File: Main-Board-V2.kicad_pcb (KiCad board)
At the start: 2 copper layers, 200 x 70 mm, 74 parts, among them IC1 REG1117-5, J2 776280-1, J3 776280-1, J4 1-776163-5, K1 J107F1AS123VDC.36, K2 J107F1AS123VDC.36, K3 J107F1AS123VDC.36, K4 J107F1AS123VDC.36, K5 J107F1AS123VDC.36, Q1 2N2222A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

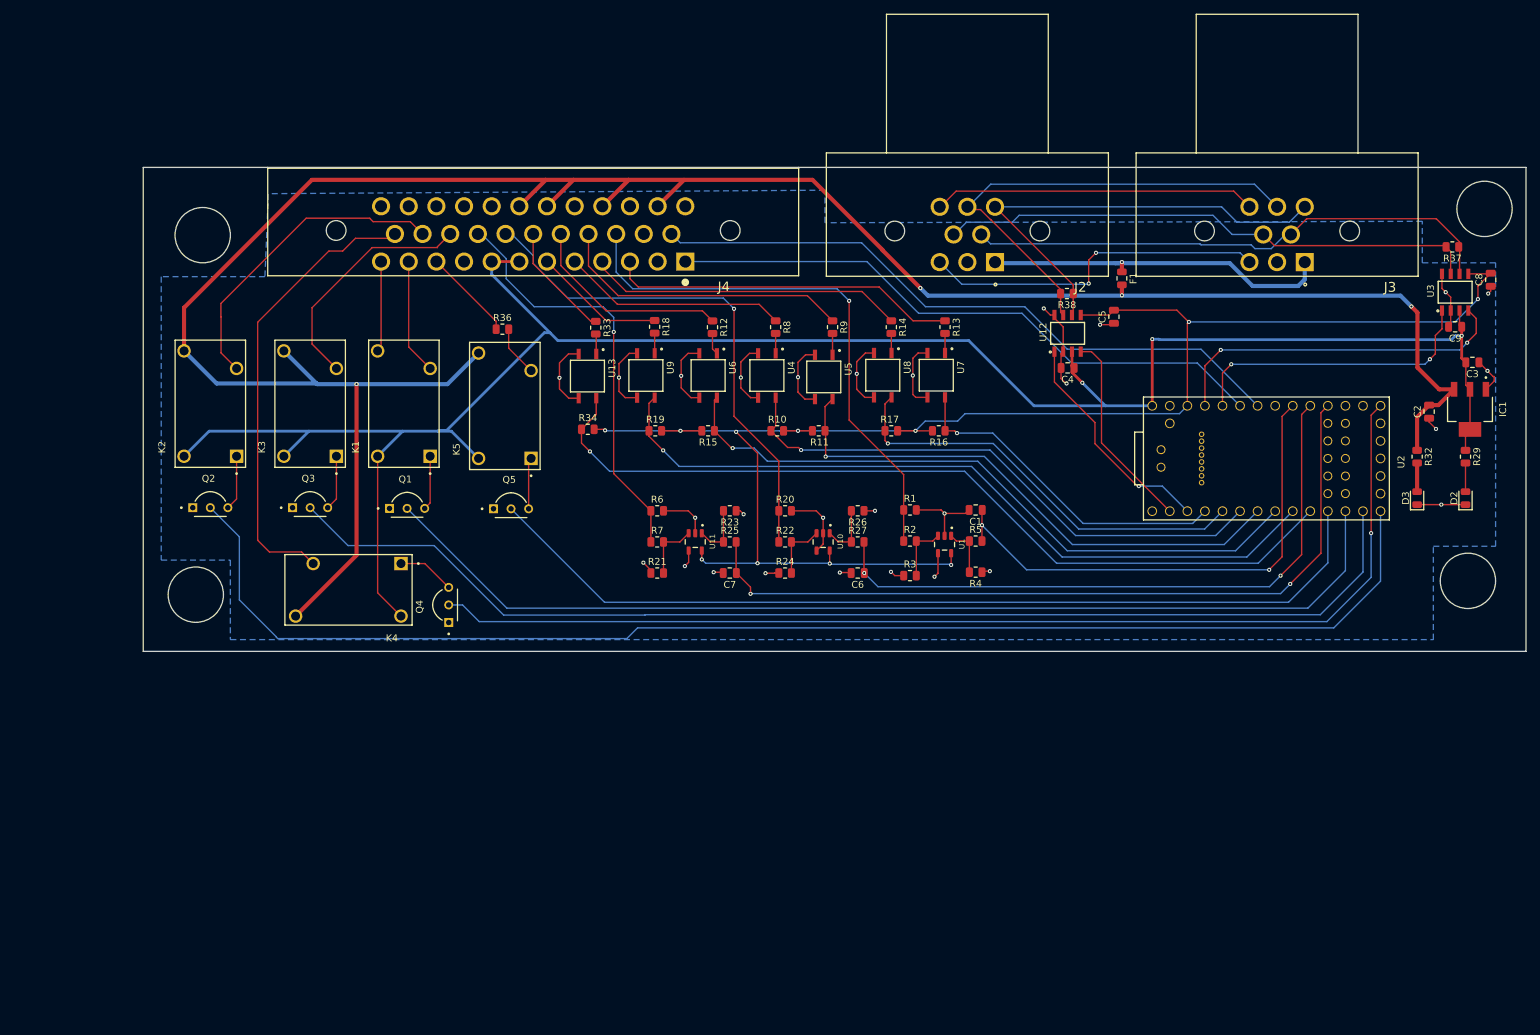
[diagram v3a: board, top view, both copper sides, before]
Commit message: fixed mounting holes
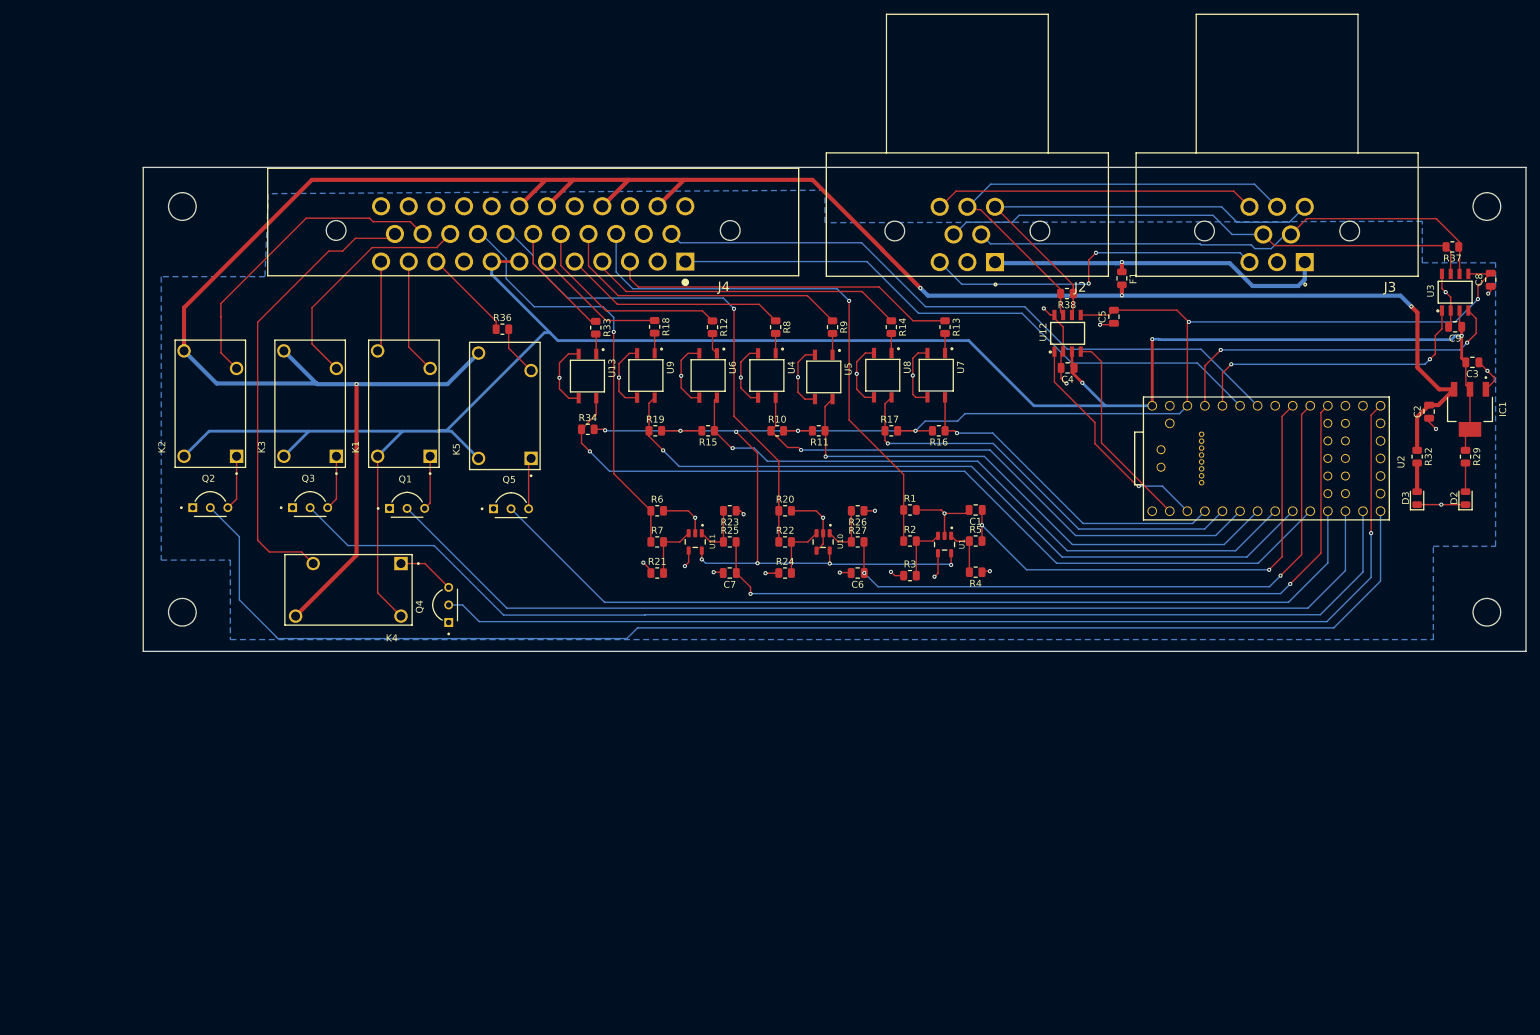
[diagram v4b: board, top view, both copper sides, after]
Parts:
- added REF**: MountingHole_4mm, MountingHole:MountingHole_4mm, F.Cu at (240.2, 125.5)
- added REF**: MountingHole_4mm, MountingHole:MountingHole_4mm, F.Cu at (240.2, 66.8)
- added REF**: MountingHole_4mm, MountingHole:MountingHole_4mm, F.Cu at (51.5, 66.8)
- added REF**: MountingHole_4mm, MountingHole:MountingHole_4mm, F.Cu at (51.5, 125.5)
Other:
- outline, holes or cut-outs redrawn

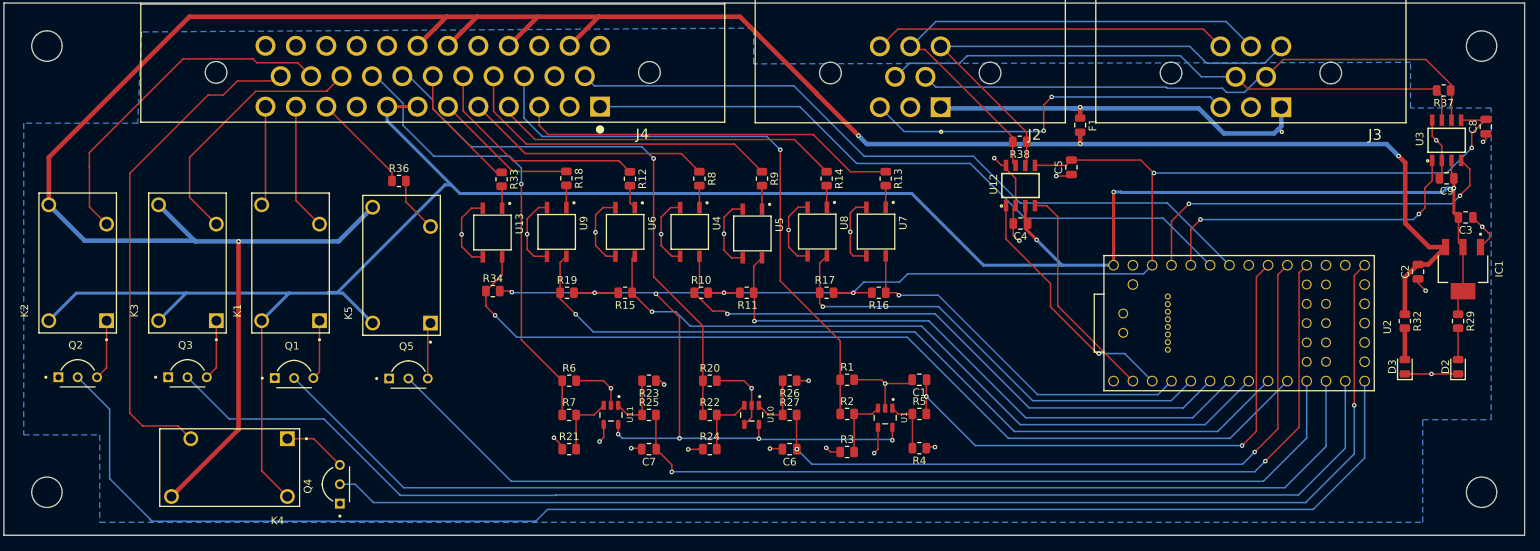
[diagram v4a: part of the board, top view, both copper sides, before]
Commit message: front silkscreen
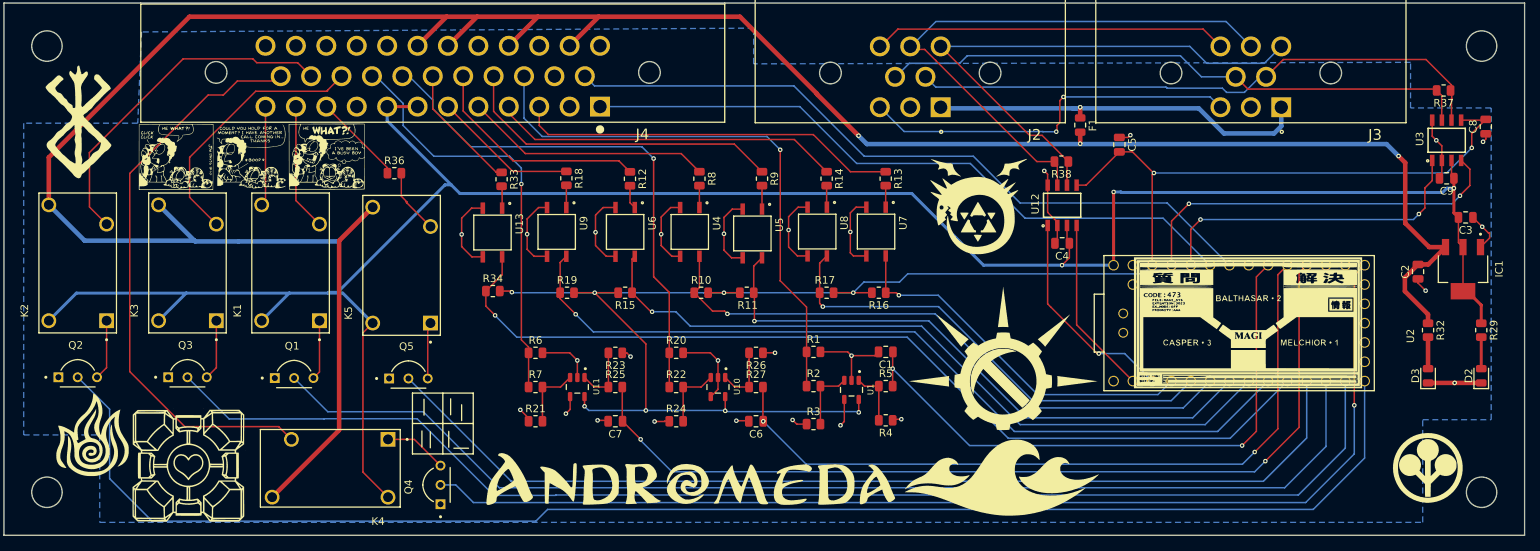
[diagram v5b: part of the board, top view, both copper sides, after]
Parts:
- removed the G*** at (142.0, 96.5)
- added G***: LOGO, LOGO, F.Cu at (177.1, 123.6)
- added G***: LOGO, LOGO, F.Cu at (174.1, 88.0)
- added G***: LOGO, LOGO, B.Cu at (212.3, 126.9)
- added G***: LOGO, LOGO, B.Cu at (233.2, 122.3)
- added G***: LOGO, LOGO, B.Cu at (126.4, 100.6)
- added G***: LOGO, LOGO, F.Cu at (177.3, 107.9)
- added G***: LOGO, LOGO, F.Cu at (209.5, 103.2)
- added G***: LOGO, LOGO, F.Cu at (57.5, 118.0)
- added G***: LOGO, LOGO, F.Cu at (78.5, 81.4)
- added G***: LOGO, LOGO, F.Cu at (70.2, 122.0)
- added G***: LOGO, LOGO, F.Cu at (55.7, 76.8)
- added G***: LOGO, LOGO, F.Cu at (233.2, 122.3)
- added G***: LOGO, LOGO, F.Cu at (136.3, 123.9)
- C1, C6, C7: value 1N -> 0.1U
- R21, R24: value 10k -> 20k
- R3: value 10k -> 30k
- R5: value 1k -> 1000R
- moved K4 13.2 mm to (88.8, 122.4)
- moved Q4 13.2 mm to (101.0, 124.6)
- moved C5 6.97 mm to (192.6, 79.8), turned to -90 degrees
- moved C4 6.07 mm to (185.1, 92.8)
- moved R38 6.07 mm to (185.0, 82.0)
- moved U12 6.07 mm to (185.1, 87.8)
- moved R21 5.75 mm to (115.8, 116.2)
- moved R6 5.75 mm to (115.8, 107.2)
- moved R7 5.75 mm to (115.8, 111.7)
- moved U11 5.75 mm to (121.3, 111.7)
- moved C7 5.75 mm to (126.3, 116.2)
- moved R23 5.75 mm to (126.3, 107.2)
- moved R25 5.75 mm to (126.3, 111.7)
- moved C1 5.75 mm to (161.9, 107.1)
- moved C6 5.75 mm to (144.8, 116.2)
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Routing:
- net /RightSignalIO: track 162.5 -> 149.2 mm
- net /Relays/RightSignal: track 65.2 -> 75.3 mm
- net +12V: track 340.1 -> 349.0 mm, vias 4 -> 3
- net /Can/CaNH1: track 69.1 -> 75.4 mm
- net /Can/CaNL1: track 66.8 -> 72.9 mm
- net /EncoderIO: track 73.8 -> 79.7 mm
- net /Throttle2IO: track 92.5 -> 98.5 mm
- net /Can_RX1: track 29.3 -> 23.5 mm
- net +3.3V: track 243.7 -> 238.1 mm, vias 11 -> 10
- net /Pedal/Throttle2: track 73.7 -> 68.2 mm
- net /Pedal/Throttle1: track 60.5 -> 55.0 mm
- net /Encoder: track 79.0 -> 73.5 mm
- net /Throttle1IO: track 115.0 -> 120.4 mm
- net /Can_TX1: track 33.1 -> 28.3 mm
- net GND: track 155.6 -> 153.3 mm, vias 28 -> 27
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
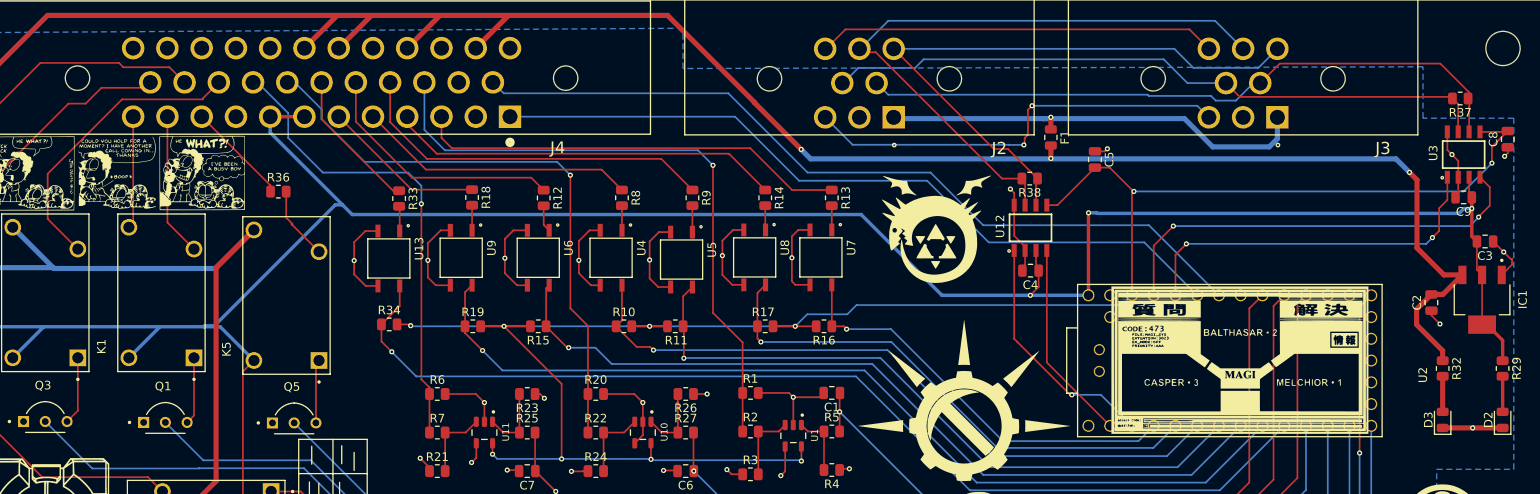
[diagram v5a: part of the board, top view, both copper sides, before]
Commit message: finished silkscreen
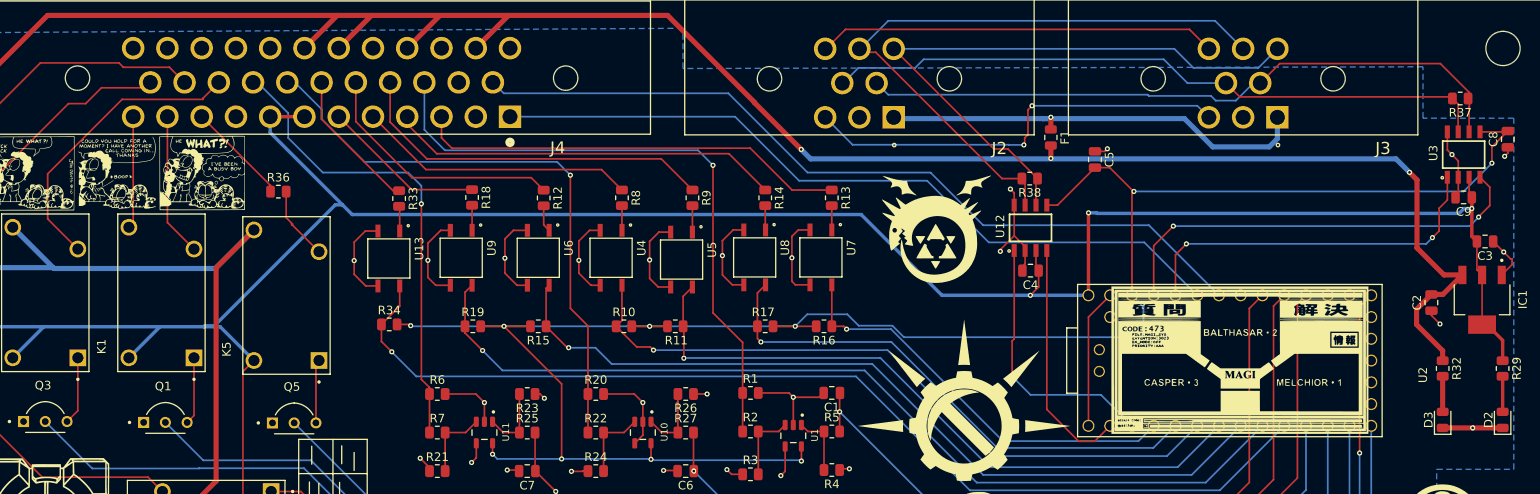
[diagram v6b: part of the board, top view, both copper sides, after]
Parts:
- added G***: LOGO, LOGO, B.Cu at (63.5, 77.0)
- added G***: LOGO, LOGO, B.Cu at (192.8, 75.5)
- added G***: LOGO, LOGO, B.Cu at (229.7, 76.1)
- added G***: LOGO, LOGO, B.Cu at (209.9, 83.4)
- added G***: LOGO, LOGO, B.Cu at (207.7, 103.3)
- added G***: LOGO, LOGO, B.Cu at (73.2, 120.8)
- moved G*** 4.54 mm to (207.7, 127.1)
- moved G*** 4.54 mm to (228.6, 122.6)
- moved G*** 4.52 mm to (129.4, 97.2)
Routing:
- net GND: track 153.3 -> 171.2 mm, vias 27 -> 28
- net +3.3V: track 238.1 -> 244.9 mm
- net /Can_RX1: track 23.5 -> 28.2 mm
- net /Can_TX1: track 28.3 -> 31.2 mm
- net +5V: track 295.6 -> 294.6 mm
- net /Can/CaNH1: track 75.4 -> 74.8 mm
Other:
- board text added: "Shinji, get in the Solar Car"

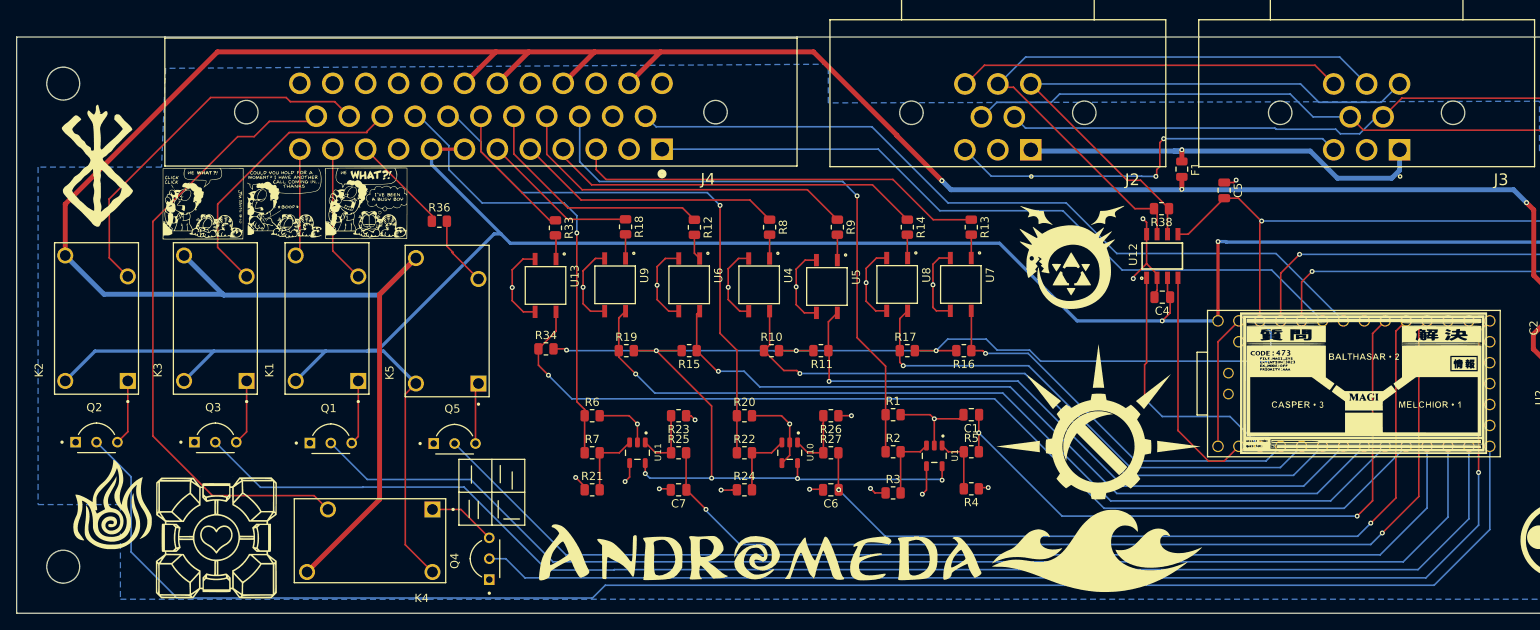
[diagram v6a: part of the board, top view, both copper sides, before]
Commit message: fixed relays
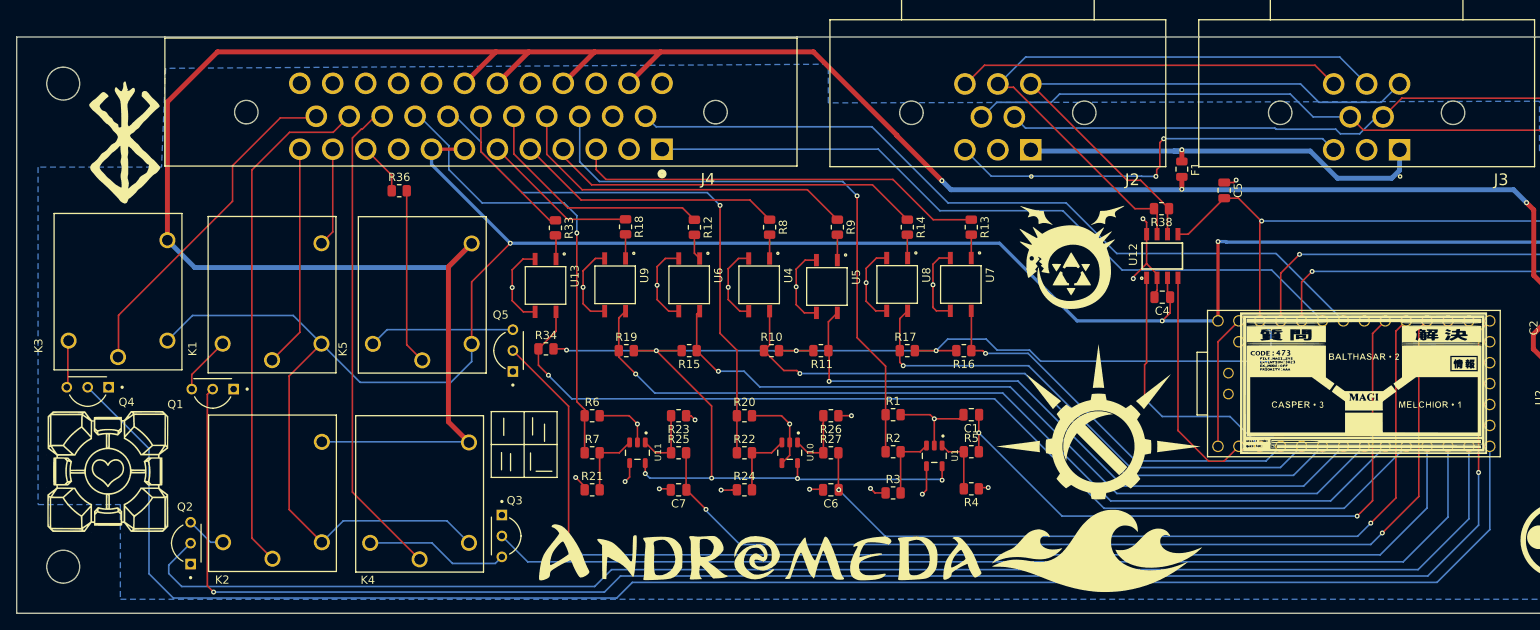
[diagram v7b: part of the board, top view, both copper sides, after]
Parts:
- removed the G*** at (57.5, 118.0)
- removed the G*** at (78.5, 81.4)
- added G***: LOGO, LOGO, B.Cu at (72.5, 90.5)
- K1, K2, K3, K4, K5: footprint PRE29-5V-S-450-1A-E:RELAY_PRE29-5V-S-450-1A-E -> J107F1AS123VDC.36:RELAY_J107F1AS123VDC.36
- moved Q4 50.0 mm to (54.5, 106.1), turned to 180 degrees
- moved Q3 39.6 mm to (107.1, 121.8), turned to -90 degrees
- moved K2 30.1 mm to (77.0, 116.6)
- moved Q2 17.2 mm to (64.7, 122.7), turned to 90 degrees
- moved G*** 15.4 mm to (57.0, 114.0)
- moved Q1 14.5 mm to (69.7, 106.3), turned to 180 degrees
- moved K3 12.3 mm to (58.2, 92.1)
- moved Q5 10.1 mm to (103.8, 99.3), turned to 90 degrees
- moved K4 8.29 mm to (94.8, 116.7), turned to 90 degrees
- moved K1 7.27 mm to (76.9, 92.5)
- moved G*** 6.84 mm to (69.3, 115.2)
- moved R36 6.12 mm to (92.4, 79.9)
- moved K5 4.39 mm to (95.2, 92.5)
- moved G*** 4.36 mm to (59.0, 74.0)
- moved G*** 2.60 mm to (63.0, 74.4)
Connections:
- Q1 pad 3: Net-(K1-Pad1) -> Net-(K1-PadCOIL1)
- Q2 pad 3: Net-(K2-Pad1) -> Net-(K2-PadCOIL1)
- Q3 pad 3: Net-(K3-Pad1) -> Net-(K4-PadCOIL1)
- Q4 pad 3: Net-(K4-Pad1) -> Net-(K3-PadCOIL1)
- Q5 pad 3: Net-(K5-Pad1) -> Net-(K5-PadCOIL1)
- R36 pad 2: Net-(K5-Pad3) -> Net-(K5-PadCOM)
- U2 pad 12: /BattRelay -> /BrakeRelay
- U2 pad 13: /BrakeRelay -> /LeftSignalIO
- U2 pad 14: /LeftSignalIO -> /RightSignalIO
- U2 pad 20: /RightSignalIO -> /BattRelay
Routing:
- net /BattRelay: track 152.5 -> 207.7 mm, vias 0 -> 2
- net /RightSignalIO: track 149.2 -> 203.4 mm, vias 1 -> 0
- net /BrakeRelay: track 170.1 -> 127.1 mm
- net /Relays/RightSignal: track 75.3 -> 41.5 mm
- net /Relays/BrakeLight: track 34.7 -> 58.4 mm
- net Net-(K5-PadCOM): track 0.00 -> 21.4 mm
- net /LeftSignalIO: track 196.0 -> 175.6 mm
- net +12V: track 349.0 -> 329.0 mm
- net Net-(K5-PadCOIL1): track 0.00 -> 17.7 mm
- net Net-(K4-PadCOIL1): track 0.00 -> 17.4 mm
- net /Relays/LeftSignal: track 45.6 -> 62.8 mm
- net /Relays/BattOut: track 12.4 -> 27.0 mm
- net Net-(K5-Pad3): track 8.79 -> 0.00 mm
- net Net-(K4-Pad1): track 8.33 -> 0.00 mm
- net Net-(K3-Pad1): track 7.96 -> 0.00 mm
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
